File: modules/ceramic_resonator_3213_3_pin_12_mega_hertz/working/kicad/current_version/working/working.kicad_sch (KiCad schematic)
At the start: 3 parts, among them x1 xcr3213mhz12

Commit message: gitignore update mainly and update
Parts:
- removed x1: xcr3213mhz12, xcr3213mhz16_electronic_ceramic_resonator_3213_3_pin_ground_pin_2_16_mega_hertz, symbol oomlout_oomp_part_symbols:xcr3213mhz16_electronic_ceramic_resonator_3213_3_pin_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
- added x1: xcr3213mhz12, xcr3213mhz12_electronic_ceramic_resonator_3213_3_pin_ground_pin_2_12_mega_hertz, symbol oomlout_oomp_part_symbols:xcr3213mhz12_electronic_ceramic_resonator_3213_3_pin_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
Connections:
- net GND: now also x1.2
- net xtal_1: now also x1.1
- net xtal_2: now also x1.3
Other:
- note added: "oomp ceramic_resonator 3213_3_pin 12_mega_hertz"
- note removed: "module ceramic_resonator 3213 3_pin 12_mega_hertz"
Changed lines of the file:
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@@
     (stroke (width 0) (type default))
+  )
+  (rectangle (start 109.22 44.45) (end 172.72 95.25)
+    (stroke (width 1) (type default))
+    (fill (type none))
+  )
+  (rectangle (start 171.45 101.6) (end 171.45 101.6)
+    (stroke (width 0) (type default))
+    (fill (type none))
+  )
+  (rectangle (start 246.38 101.6) (end 246.38 101.6)
+    (stroke (width 0) (type default))
+    (fill (type none))
   )
   (rectangle (start 134.62 44.45) (end 172.72 50.8)
@@
     (fill (type color) (color 0 0 0 0))
   )
-  (rectangle (start 171.45 101.6) (end 171.45 101.6)
-    (stroke (width 0) (type default))
-    (fill (type none))
-  )
-  (rectangle (start 109.22 44.45) (end 172.72 95.25)
-    (stroke (width 1) (type default))
-    (fill (type none))
-  )
   (text "xcr" (at 171.45 50.8 0)
     (effects (font (size 4 4) (thickness 0.8) bold (color 255 255 255 1)) (justify right bottom))
   )
+  (text "oomp\nceramic_resonator\n3213_3_pin\n12_mega_hertz\n\n" (at 110.49 67.31 0)
+    (effects (font (size 2.5 2.5)) (justify left bottom))
+  )
   (text "name" (at 137.16 50.8 90)
     (effects (font (size 1.27 1.27) (thickness 0.254) bold (color 255 255 255 1)) (justify left bottom))
-  )
-  (text "module\nceramic_resonator\n3213\n3_pin\n12_mega_hertz\n\n"
-    (at 110.49 71.12 0)
-    (effects (font (size 2.5 2.5)) (justify left bottom))
   )
   (label "xtal_2" (at 153.67 76.2 0) (fields_autoplaced)
@@
     )
   )
+  (symbol (lib_id "oomlout_oomp_part_symbols:xcr3213mhz12_electronic_ceramic_resonator_3213_3_pin_ground_pin_2_12_mega_hertz") (at 140.97 76.2 0) (unit 1)
+    (in_bom yes) (on_board yes) (dnp no) (fields_autoplaced)
+    (property "Reference" "x1" (at 140.97 68.58 0)
+      (effects (font (size 1.27 1.27)))
+    )
+    (property "Value" "xcr3213mhz12" (at 140.97 71.12 0)
+      (effects (font (size 1.27 1.27)))
+    )
+    (property "Footprint" "xcr3213mhz12_electronic_ceramic_resonator_3213_3_pin_ground_pin_2_12_mega_hertz" (at 140.97 76.2 0)
+      (effects (font (size 1.27 1.27)) hide)
+    )
+    (property "Datasheet" "https://github.com/oomlout/oomlout_oomp_v3/parts/electronic_ceramic_resonator_3213_3_pin_ground_pin_2_12_mega_hertz/datasheet.pdf" (at 140.97 76.2 0)
+      (effects (font (size 1.27 1.27)) hide)
+    )
+    (pin "1")
+    (pin "2")
+    (pin "3")
+    (instances
+      (project "working"
+        (path "/3a6aff3f-64f2-4c1e-bb10-1dc442a40a0c"
+          (reference "x1") (unit 1)
+        )
+      )
+    )
+  )
   (symbol (lib_id "power:GND") (at 140.97 87.63 0) (unit 1)
     (in_bom yes) (on_board yes) (dnp no) (fields_autoplaced)
@@
         )
       )
-    )
-  )
-  (symbol (lib_id "oomlout_oomp_part_symbols:xcr3213mhz16_electronic_ceramic_resonator_3213_3_pin_ground_pin_2_16_mega_hertz") (at 140.97 76.2 0) (unit 1)
-    (in_bom yes) (on_board yes) (dnp no) (fields_autoplaced)
-    (property "Reference" "x1" (at 140.97 68.58 0)
-      (effects (font (size 1.27 1.27)))
-    )
-    (property "Value" "xcr3213mhz12" (at 140.97 71.12 0)
-      (effects (font (size 1.27 1.27)))
-    )
-    (property "Footprint" "xcr3213mhz16_electronic_ceramic_resonator_3213_3_pin_ground_pin_2_16_mega_hertz" (at 140.97 76.2 0)
-      (effects (font (size 1.27 1.27)) hide)
-    )
-    (property "Datasheet" "https://github.com/oomlout/oomlout_oomp_v3/parts/electronic_ceramic_resonator_3213_3_pin_ground_pin_2_16_mega_hertz/datasheet.pdf" (at 140.97 76.2 0)
-      (effects (font (size 1.27 1.27)) hide)
-    )
-    (pin "1")
-    (pin "2")
-    (pin "3")
-    (instances
-      (project "working"
-        (path "/3a6aff3f-64f2-4c1e-bb10-1dc442a40a0c"
-          (reference "x1") (unit 1)
-        )
-      )

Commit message: a few module workings
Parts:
- removed C1, C2: c6pf22, c6pf22_electronic_capacitor_0603_22_pico_farad, symbol oomlout_oomp_part_symbols:c6pf22_electronic_capacitor_0603_22_pico_farad
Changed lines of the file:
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@@
 (kicad_sch (version 20230121) (generator eeschema)
   (paper "A4")
-  (junction (at 140.97 87.63) (diameter 0) (color 0 0 0 0)
-  )
-  (junction (at 151.13 76.2) (diameter 0) (color 0 0 0 0)
-  )
-  (junction (at 130.81 76.2) (diameter 0) (color 0 0 0 0)
-  )
-  (wire (pts (xy 130.81 87.63) (xy 140.97 87.63))
-    (stroke (width 0) (type default))
-  )
-  (wire (pts (xy 151.13 87.63) (xy 151.13 86.36))
-    (stroke (width 0) (type default))
-  )
-  (wire (pts (xy 140.97 87.63) (xy 151.13 87.63))
-    (stroke (width 0) (type default))
-  )
-  (wire (pts (xy 130.81 86.36) (xy 130.81 87.63))
-    (stroke (width 0) (type default))
-  )
   (wire (pts (xy 140.97 81.28) (xy 140.97 87.63))
     (stroke (width 0) (type default))
   )
-  (wire (pts (xy 151.13 76.2) (xy 151.13 78.74))
+  (wire (pts (xy 128.27 76.2) (xy 137.16 76.2))
     (stroke (width 0) (type default))
   )
-  (wire (pts (xy 128.27 76.2) (xy 130.81 76.2))
-    (stroke (width 0) (type default))
-  )
-  (wire (pts (xy 130.81 76.2) (xy 137.16 76.2))
-    (stroke (width 0) (type default))
-  )
-  (wire (pts (xy 130.81 76.2) (xy 130.81 78.74))
-    (stroke (width 0) (type default))
-  )
-  (wire (pts (xy 151.13 76.2) (xy 153.67 76.2))
-    (stroke (width 0) (type default))
-  )
-  (wire (pts (xy 144.78 76.2) (xy 151.13 76.2))
+  (wire (pts (xy 144.78 76.2) (xy 153.67 76.2))
     (stroke (width 0) (type default))
   )
@@
     (effects (font (size 1.27 1.27)) (justify right bottom))
   )
-  (symbol (lib_id "oomlout_oomp_part_symbols:c6pf22_electronic_capacitor_0603_22_pico_farad") (at 130.81 82.55 0) (unit 1)
-    (in_bom yes) (on_board yes) (dnp no)
-    (property "Reference" "C1" (at 124.46 81.28 0)
-      (effects (font (size 1.27 1.27)) (justify left))
-    )
-    (property "Value" "c6pf22" (at 120.65 83.82 0)
-      (effects (font (size 1.27 1.27)) (justify left))
-    )
-    (property "Footprint" "c6pf22_electronic_capacitor_0603_22_pico_farad" (at 131.7752 86.36 0)
-      (effects (font (size 1.27 1.27)) hide)
-    )
-    (property "Datasheet" "https://github.com/oomlout/oomlout_oomp_v3/parts/electronic_capacitor_0603_22_pico_farad/datasheet.pdf" (at 130.81 82.55 0)
-      (effects (font (size 1.27 1.27)) hide)
-    )
-    (pin "1")
-    (pin "2")
-    (instances
-      (project "working"
-        (path "/3a6aff3f-64f2-4c1e-bb10-1dc442a40a0c"
-          (reference "C1") (unit 1)
-        )
-      )
-    )
-  )
-  (symbol (lib_id "oomlout_oomp_part_symbols:c6pf22_electronic_capacitor_0603_22_pico_farad") (at 151.13 82.55 0) (unit 1)
-    (in_bom yes) (on_board yes) (dnp no)
-    (property "Reference" "C2" (at 154.94 81.28 0)
-      (effects (font (size 1.27 1.27)) (justify left))
-    )
-    (property "Value" "c6pf22" (at 154.94 83.82 0)
-      (effects (font (size 1.27 1.27)) (justify left))
-    )
-    (property "Footprint" "c6pf22_electronic_capacitor_0603_22_pico_farad" (at 152.0952 86.36 0)
-      (effects (font (size 1.27 1.27)) hide)
-    )
-    (property "Datasheet" "https://github.com/oomlout/oomlout_oomp_v3/parts/electronic_capacitor_0603_22_pico_farad/datasheet.pdf" (at 151.13 82.55 0)
-      (effects (font (size 1.27 1.27)) hide)
-    )
-    (pin "1")
-    (pin "2")
-    (instances
-      (project "working"
-        (path "/3a6aff3f-64f2-4c1e-bb10-1dc442a40a0c"
-          (reference "C2") (unit 1)
-        )
-      )
-    )
-  )
   (symbol (lib_id "oomlout_oomp_part_symbols:xcr3213mhz12_electronic_ceramic_resonator_3213_3_pin_ground_pin_2_12_mega_hertz") (at 140.97 76.2 0) (unit 1)

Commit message: a few module fixes
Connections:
- net xtal_1 renamed xtal1
- net xtal_2 renamed xtal2
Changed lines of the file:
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@@
     (effects (font (size 1.27 1.27) (thickness 0.254) bold (color 255 255 255 1)) (justify left bottom))
   )
-  (label "xtal_2" (at 153.67 76.2 0) (fields_autoplaced)
+  (label "xtal2" (at 153.67 76.2 0) (fields_autoplaced)
     (effects (font (size 1.27 1.27)) (justify left bottom))
   )
-  (label "xtal_1" (at 128.27 76.2 180) (fields_autoplaced)
+  (label "xtal1" (at 128.27 76.2 180) (fields_autoplaced)
     (effects (font (size 1.27 1.27)) (justify right bottom))
   )

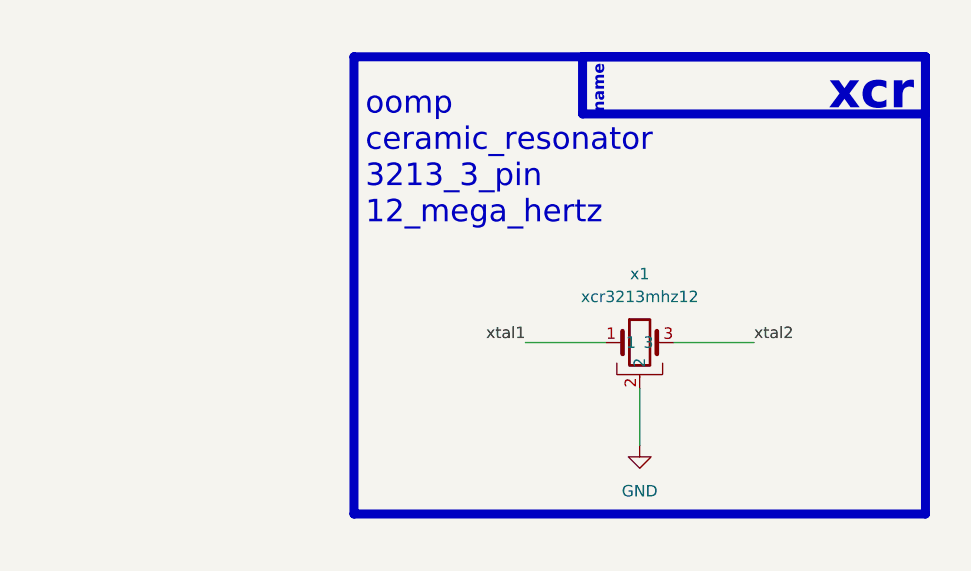
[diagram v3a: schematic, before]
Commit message: fixed formatting to be more consistent
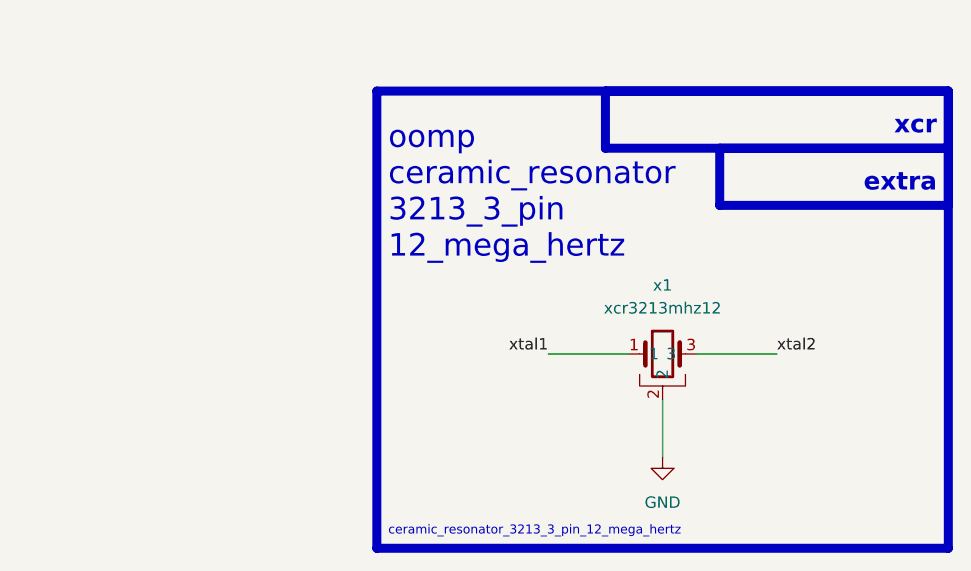
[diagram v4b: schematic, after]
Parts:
- x1: footprint xcr3213mhz12_electronic_ceramic_resonator_3213_3_pin_ground_pin_2_12_mega_hertz -> oomlout_oomp_part_footprints:xcr3213mhz12_electronic_ceramic_resonator_3213_3_pin_ground_pin_2_12_mega_hertz
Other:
- note added: "ceramic_resonator_3213_3_pin_12_mega_hertz"
- note added: "extra"
- note removed: "name"
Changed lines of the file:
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@@
 (kicad_sch (version 20230121) (generator eeschema)
   (paper "A4")
-  (wire (pts (xy 140.97 81.28) (xy 140.97 87.63))
+  (wire (pts (xy 130.81 77.47) (xy 139.7 77.47))
     (stroke (width 0) (type default))
   )
-  (wire (pts (xy 128.27 76.2) (xy 137.16 76.2))
+  (wire (pts (xy 143.51 82.55) (xy 143.51 88.9))
     (stroke (width 0) (type default))
   )
-  (wire (pts (xy 144.78 76.2) (xy 153.67 76.2))
+  (wire (pts (xy 147.32 77.47) (xy 156.21 77.47))
     (stroke (width 0) (type default))
   )
-  (rectangle (start 109.22 44.45) (end 172.72 95.25)
+  (rectangle (start 137.16 48.26) (end 175.26 54.61)
     (stroke (width 1) (type default))
+    (fill (type none))
+  )
+  (rectangle (start 173.99 105.41) (end 173.99 105.41)
+    (stroke (width 0) (type default))
     (fill (type none))
   )
@@
     (fill (type none))
   )
-  (rectangle (start 134.62 44.45) (end 172.72 50.8)
+  (rectangle (start 111.76 48.26) (end 175.26 99.06)
     (stroke (width 1) (type default))
-    (fill (type color) (color 0 0 0 0))
+    (fill (type none))
   )
-  (text "xcr" (at 171.45 50.8 0)
-    (effects (font (size 4 4) (thickness 0.8) bold (color 255 255 255 1)) (justify right bottom))
+  (rectangle (start 149.86 54.61) (end 175.26 60.96)
+    (stroke (width 1) (type default))
+    (fill (type none))
   )
-  (text "oomp\nceramic_resonator\n3213_3_pin\n12_mega_hertz\n\n" (at 110.49 67.31 0)
+  (text "oomp\nceramic_resonator\n3213_3_pin\n12_mega_hertz\n\n" (at 113.03 71.12 0)
     (effects (font (size 2.5 2.5)) (justify left bottom))
   )
-  (text "name" (at 137.16 50.8 90)
-    (effects (font (size 1.27 1.27) (thickness 0.254) bold (color 255 255 255 1)) (justify left bottom))
+  (text "xcr" (at 173.99 53.34 0)
+    (effects (font (size 2 2) (thickness 0.8) bold) (justify right bottom))
   )
-  (label "xtal2" (at 153.67 76.2 0) (fields_autoplaced)
+  (text "ceramic_resonator_3213_3_pin_12_mega_hertz" (at 113.03 97.79 0)
+    (effects (font (size 1 1)) (justify left bottom))
+  )
+  (text "extra" (at 173.99 59.69 0)
+    (effects (font (size 2 2) (thickness 0.8) bold) (justify right bottom))
+  )
+  (label "xtal2" (at 156.21 77.47 0) (fields_autoplaced)
     (effects (font (size 1.27 1.27)) (justify left bottom))
   )
-  (label "xtal1" (at 128.27 76.2 180) (fields_autoplaced)
+  (label "xtal1" (at 130.81 77.47 180) (fields_autoplaced)
     (effects (font (size 1.27 1.27)) (justify right bottom))
   )
-  (symbol (lib_id "oomlout_oomp_part_symbols:xcr3213mhz12_electronic_ceramic_resonator_3213_3_pin_ground_pin_2_12_mega_hertz") (at 140.97 76.2 0) (unit 1)
+  (symbol (lib_id "oomlout_oomp_part_symbols:xcr3213mhz12_electronic_ceramic_resonator_3213_3_pin_ground_pin_2_12_mega_hertz") (at 143.51 77.47 0) (unit 1)
     (in_bom yes) (on_board yes) (dnp no) (fields_autoplaced)
-    (property "Reference" "x1" (at 140.97 68.58 0)
+    (property "Reference" "x1" (at 143.51 69.85 0)
       (effects (font (size 1.27 1.27)))
     )
-    (property "Value" "xcr3213mhz12" (at 140.97 71.12 0)
+    (property "Value" "xcr3213mhz12" (at 143.51 72.39 0)
       (effects (font (size 1.27 1.27)))
     )
-    (property "Footprint" "xcr3213mhz12_electronic_ceramic_resonator_3213_3_pin_ground_pin_2_12_mega_hertz" (at 140.97 76.2 0)
+    (property "Footprint" "oomlout_oomp_part_footprints:xcr3213mhz12_electronic_ceramic_resonator_3213_3_pin_ground_pin_2_12_mega_hertz" (at 143.51 77.47 0)
       (effects (font (size 1.27 1.27)) hide)
     )
-    (property "Datasheet" "https://github.com/oomlout/oomlout_oomp_v3/parts/electronic_ceramic_resonator_3213_3_pin_ground_pin_2_12_mega_hertz/datasheet.pdf" (at 140.97 76.2 0)
+    (property "Datasheet" "https://github.com/oomlout/oomlout_oomp_v3/parts/electronic_ceramic_resonator_3213_3_pin_ground_pin_2_12_mega_hertz/datasheet.pdf" (at 143.51 77.47 0)
       (effects (font (size 1.27 1.27)) hide)
     )
@@
     )
   )
-  (symbol (lib_id "power:GND") (at 140.97 87.63 0) (unit 1)
+  (symbol (lib_id "power:GND") (at 143.51 88.9 0) (unit 1)
     (in_bom yes) (on_board yes) (dnp no) (fields_autoplaced)
-    (property "Reference" "#PWR02" (at 140.97 93.98 0)
+    (property "Reference" "#PWR01" (at 143.51 95.25 0)
       (effects (font (size 1.27 1.27)) hide)
     )
-    (property "Value" "GND" (at 140.97 92.71 0)
+    (property "Value" "GND" (at 143.51 93.98 0)
       (effects (font (size 1.27 1.27)))
     )
-    (property "Footprint" "" (at 140.97 87.63 0)
+    (property "Footprint" "" (at 143.51 88.9 0)
       (effects (font (size 1.27 1.27)) hide)
     )
-    (property "Datasheet" "" (at 140.97 87.63 0)
+    (property "Datasheet" "" (at 143.51 88.9 0)
       (effects (font (size 1.27 1.27)) hide)
     )
@@
       (project "working"
         (path "/3a6aff3f-64f2-4c1e-bb10-1dc442a40a0c"
-          (reference "#PWR02") (unit 1)
+          (reference "#PWR01") (unit 1)
         )
       )

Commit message: schematic formatting
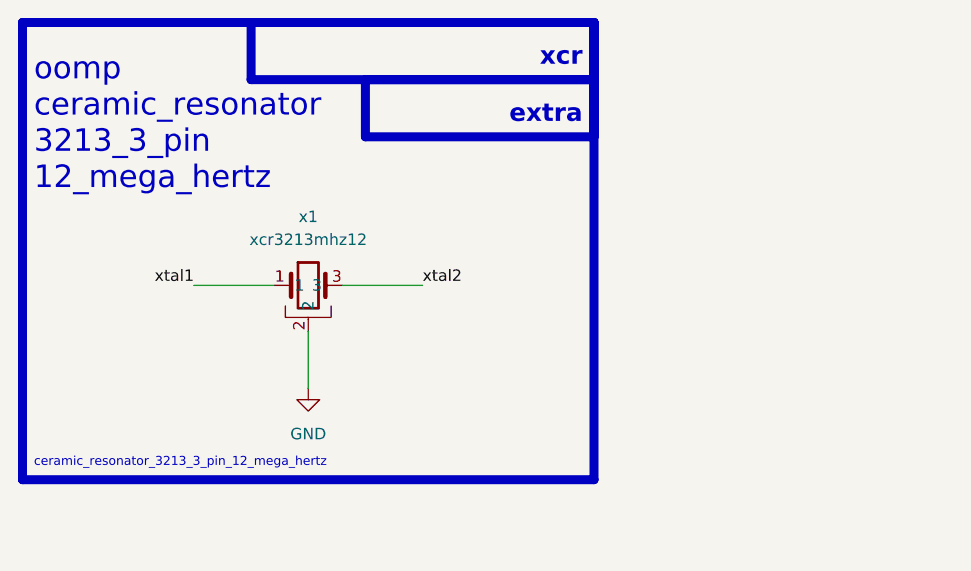
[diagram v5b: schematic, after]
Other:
- moved on the sheet: x1
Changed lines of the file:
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@@
 (kicad_sch (version 20230121) (generator eeschema)
-  (paper "A4")
-  (wire (pts (xy 130.81 77.47) (xy 139.7 77.47))
+  (paper "A5")
+  (wire (pts (xy 91.44 69.85) (xy 100.33 69.85))
     (stroke (width 0) (type default))
   )
-  (wire (pts (xy 143.51 82.55) (xy 143.51 88.9))
+  (wire (pts (xy 104.14 74.93) (xy 104.14 81.28))
     (stroke (width 0) (type default))
   )
-  (wire (pts (xy 147.32 77.47) (xy 156.21 77.47))
+  (wire (pts (xy 107.95 69.85) (xy 116.84 69.85))
     (stroke (width 0) (type default))
   )
-  (rectangle (start 137.16 48.26) (end 175.26 54.61)
+  (rectangle (start 97.79 40.64) (end 135.89 46.99)
     (stroke (width 1) (type default))
     (fill (type none))
   )
-  (rectangle (start 173.99 105.41) (end 173.99 105.41)
+  (rectangle (start 134.62 97.79) (end 134.62 97.79)
     (stroke (width 0) (type default))
     (fill (type none))
   )
-  (rectangle (start 171.45 101.6) (end 171.45 101.6)
+  (rectangle (start 132.08 93.98) (end 132.08 93.98)
     (stroke (width 0) (type default))
     (fill (type none))
   )
-  (rectangle (start 246.38 101.6) (end 246.38 101.6)
+  (rectangle (start 207.01 93.98) (end 207.01 93.98)
     (stroke (width 0) (type default))
     (fill (type none))
   )
-  (rectangle (start 111.76 48.26) (end 175.26 99.06)
+  (rectangle (start 72.39 40.64) (end 135.89 91.44)
     (stroke (width 1) (type default))
     (fill (type none))
   )
-  (rectangle (start 149.86 54.61) (end 175.26 60.96)
+  (rectangle (start 110.49 46.99) (end 135.89 53.34)
     (stroke (width 1) (type default))
     (fill (type none))
   )
-  (text "oomp\nceramic_resonator\n3213_3_pin\n12_mega_hertz\n\n" (at 113.03 71.12 0)
+  (text "oomp\nceramic_resonator\n3213_3_pin\n12_mega_hertz\n\n" (at 73.66 63.5 0)
     (effects (font (size 2.5 2.5)) (justify left bottom))
   )
-  (text "xcr" (at 173.99 53.34 0)
+  (text "xcr" (at 134.62 45.72 0)
     (effects (font (size 2 2) (thickness 0.8) bold) (justify right bottom))
   )
-  (text "ceramic_resonator_3213_3_pin_12_mega_hertz" (at 113.03 97.79 0)
+  (text "ceramic_resonator_3213_3_pin_12_mega_hertz" (at 73.66 90.17 0)
     (effects (font (size 1 1)) (justify left bottom))
   )
-  (text "extra" (at 173.99 59.69 0)
+  (text "extra" (at 134.62 52.07 0)
     (effects (font (size 2 2) (thickness 0.8) bold) (justify right bottom))
   )
-  (label "xtal2" (at 156.21 77.47 0) (fields_autoplaced)
+  (label "xtal2" (at 116.84 69.85 0) (fields_autoplaced)
     (effects (font (size 1.27 1.27)) (justify left bottom))
   )
-  (label "xtal1" (at 130.81 77.47 180) (fields_autoplaced)
+  (label "xtal1" (at 91.44 69.85 180) (fields_autoplaced)
     (effects (font (size 1.27 1.27)) (justify right bottom))
   )
-  (symbol (lib_id "oomlout_oomp_part_symbols:xcr3213mhz12_electronic_ceramic_resonator_3213_3_pin_ground_pin_2_12_mega_hertz") (at 143.51 77.47 0) (unit 1)
+  (symbol (lib_id "oomlout_oomp_part_symbols:xcr3213mhz12_electronic_ceramic_resonator_3213_3_pin_ground_pin_2_12_mega_hertz") (at 104.14 69.85 0) (unit 1)
     (in_bom yes) (on_board yes) (dnp no) (fields_autoplaced)
-    (property "Reference" "x1" (at 143.51 69.85 0)
+    (property "Reference" "x1" (at 104.14 62.23 0)
       (effects (font (size 1.27 1.27)))
     )
-    (property "Value" "xcr3213mhz12" (at 143.51 72.39 0)
+    (property "Value" "xcr3213mhz12" (at 104.14 64.77 0)
       (effects (font (size 1.27 1.27)))
     )
-    (property "Footprint" "oomlout_oomp_part_footprints:xcr3213mhz12_electronic_ceramic_resonator_3213_3_pin_ground_pin_2_12_mega_hertz" (at 143.51 77.47 0)
+    (property "Footprint" "oomlout_oomp_part_footprints:xcr3213mhz12_electronic_ceramic_resonator_3213_3_pin_ground_pin_2_12_mega_hertz" (at 104.14 69.85 0)
       (effects (font (size 1.27 1.27)) hide)
     )
-    (property "Datasheet" "https://github.com/oomlout/oomlout_oomp_v3/parts/electronic_ceramic_resonator_3213_3_pin_ground_pin_2_12_mega_hertz/datasheet.pdf" (at 143.51 77.47 0)
+    (property "Datasheet" "https://github.com/oomlout/oomlout_oomp_v3/parts/electronic_ceramic_resonator_3213_3_pin_ground_pin_2_12_mega_hertz/datasheet.pdf" (at 104.14 69.85 0)
       (effects (font (size 1.27 1.27)) hide)
     )
@@
     )
   )
-  (symbol (lib_id "power:GND") (at 143.51 88.9 0) (unit 1)
+  (symbol (lib_id "power:GND") (at 104.14 81.28 0) (unit 1)
     (in_bom yes) (on_board yes) (dnp no) (fields_autoplaced)
-    (property "Reference" "#PWR01" (at 143.51 95.25 0)
+    (property "Reference" "#PWR01" (at 104.14 87.63 0)
       (effects (font (size 1.27 1.27)) hide)
     )
-    (property "Value" "GND" (at 143.51 93.98 0)
+    (property "Value" "GND" (at 104.14 86.36 0)
       (effects (font (size 1.27 1.27)))
     )
-    (property "Footprint" "" (at 143.51 88.9 0)
+    (property "Footprint" "" (at 104.14 81.28 0)
       (effects (font (size 1.27 1.27)) hide)
     )
-    (property "Datasheet" "" (at 143.51 88.9 0)
+    (property "Datasheet" "" (at 104.14 81.28 0)
       (effects (font (size 1.27 1.27)) hide)
     )
